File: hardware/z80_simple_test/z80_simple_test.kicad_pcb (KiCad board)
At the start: 2 copper layers, 95 x 100 mm, 50 parts, among them J1 Barrel_Jack_Switch, J2 Conn_02x15_Odd_Even, U1 Z84C000XPEG, U2 SRAM_512K8B_DIP_SOP_SOJ, U3 EEPROM_512K8B_DIP, U4 74XX138, U5 Z84C40XPEG, U6 74XX32, U7 74XX00

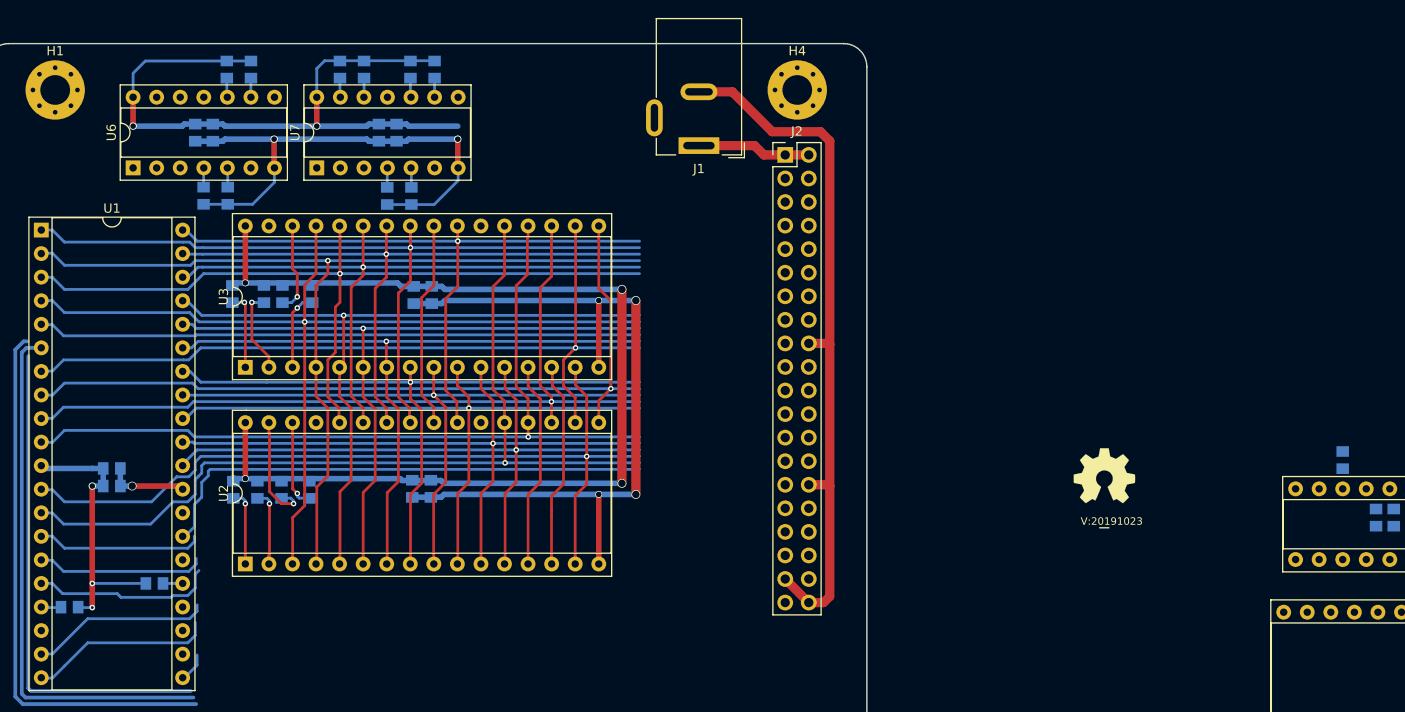
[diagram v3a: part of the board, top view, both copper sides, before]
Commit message: futher layout of the mainboard bus, replaced footprints of resistors with a bit more compact 0805/0603 universal footprint
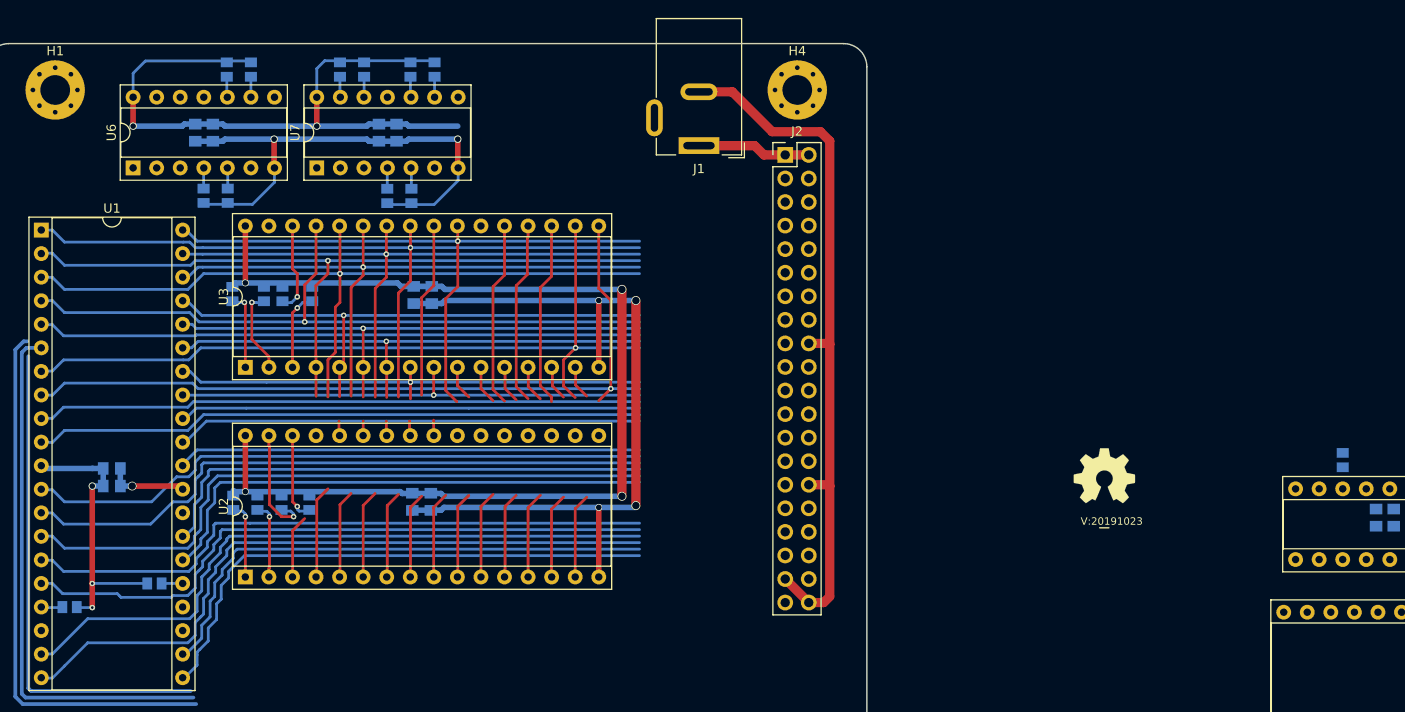
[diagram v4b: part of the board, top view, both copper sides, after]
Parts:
- R1, R10, R11, R12, R13, R14, R15, R16, R17, R18, R19, R2, R20, R21, R3, R4, R5, R6, R7, R8, R9: footprint SquantorRcl:C_0805+0603 -> SquantorRcl:R_0805+0603
- moved C3 1.40 mm to (148.5, 99.4)
- moved C4 1.40 mm to (150.5, 99.4)
- moved R4 1.40 mm to (131.8, 99.5)
- moved R5 1.40 mm to (129.2, 99.5)
- moved R6 1.40 mm to (137.4, 99.5)
- moved R7 1.40 mm to (134.4, 99.5)
- moved U2 1.40 mm to (130.5, 107.5)
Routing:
- net /!WR: track 1.18 -> 58.5 mm
- net /!RD: track 3.52 -> 58.9 mm
- net /!RESET: track 0.30 -> 55.4 mm
- net /!IORQ: track 19.9 -> 74.0 mm
- net /!MREQ: track 19.4 -> 72.5 mm
- net /!INT: track 19.7 -> 70.1 mm
- net /D0: track 40.2 -> 84.3 mm
- net /D1: track 40.4 -> 81.4 mm
- net /A14: track 103.0 -> 83.2 mm
- net /A3: track 71.6 -> 61.6 mm
- net /A4: track 72.2 -> 62.6 mm
- net /A5: track 74.6 -> 65.0 mm
- net /A7: track 77.9 -> 68.4 mm
- net /A6: track 76.0 -> 66.4 mm
- net /D2: track 89.8 -> 80.3 mm, vias 1 -> 0
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
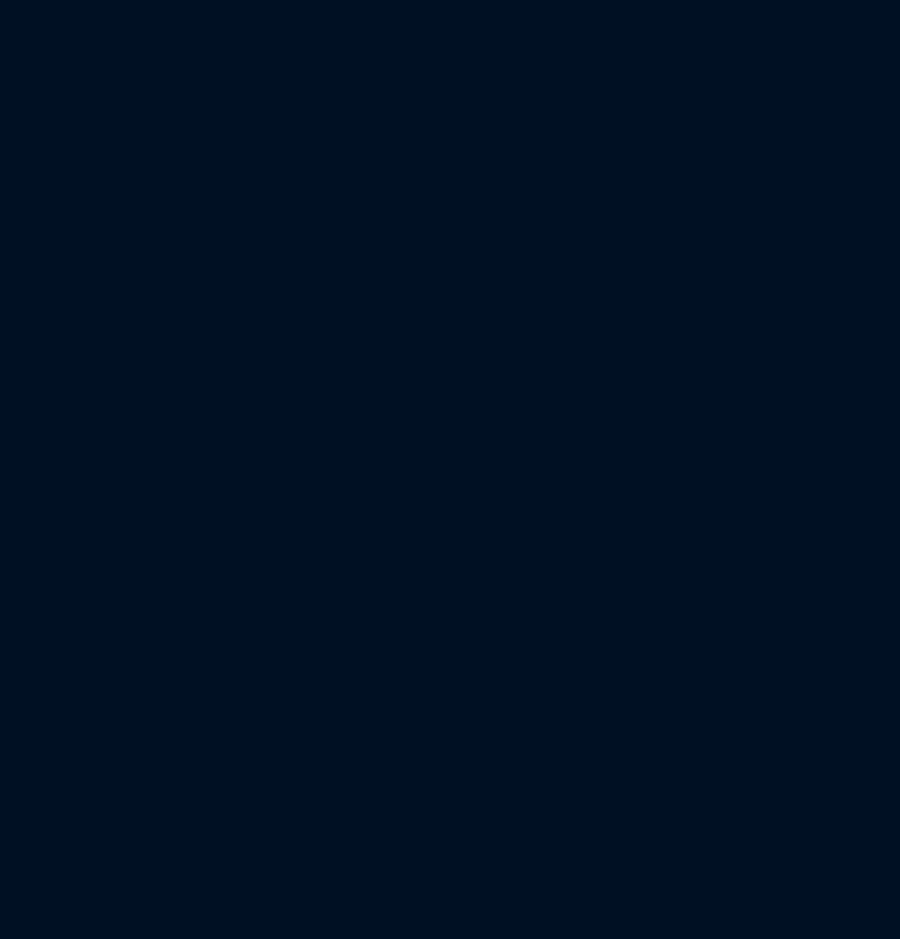
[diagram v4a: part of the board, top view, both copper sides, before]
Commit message: added power switch, need to rethink layout (again)
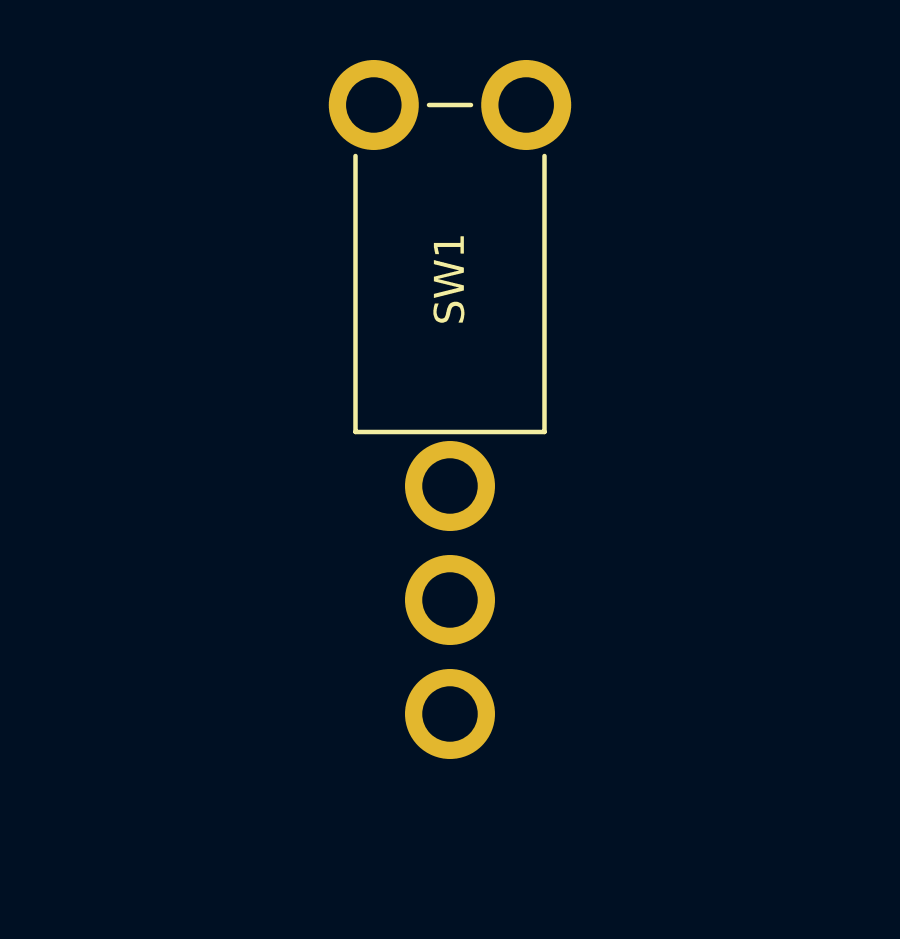
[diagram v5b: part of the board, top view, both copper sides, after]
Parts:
- added SW1: SW_Push_SPDT, SquantorSwitches:MS_500AVT, F.Cu at (227.2, 61.4)
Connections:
- J1 pad 1: /VDD -> Net-(J1-Pad1)
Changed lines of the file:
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@@
     (tracks 646)
     (zones 0)
-    (modules 50)
-    (nets 62)
+    (modules 51)
+    (nets 63)
   )
   (page A4)
@@
   (net 60 "Net-(R21-Pad2)")
   (net 61 /!RAM_CE)
+  (net 62 "Net-(J1-Pad1)")
   (net_class Default "This is the default net class."
     (clearance 0.2)
@@
     (add_net /D7)
     (add_net /SEL_SIO)
+    (add_net "Net-(J1-Pad1)")
     (add_net "Net-(J1-Pad3)")
     (add_net "Net-(R1-Pad2)")
@@
     (add_net "Net-(R20-Pad2)")
     (add_net "Net-(R21-Pad2)")
+    (add_net "Net-(SW1-Pad3)")
     (add_net "Net-(U1-Pad23)")
     (add_net "Net-(U1-Pad28)")
@@
     (add_net /VSS)
   )
+  (module SquantorSwitches:MS_500AVT (layer F.Cu)
+    (at 227.2 61.4 270)
+    (fp_text reference SW1 (at -6.9 0 90) (layer F.SilkS)
+      (effects (font (size 1 1) (thickness 0.15)))
+    )
+    (fp_text value SW_Push_SPDT (at 0 -0.5 90) (layer F.Fab)
+      (effects (font (size 1 1) (thickness 0.15)))
+    )
+    (fp_line (start -11 -3.15) (end -1.8 -3.15) (layer F.SilkS) (width 0.15))
+    (fp_line (start -12.7 0.7) (end -12.7 -0.7) (layer F.SilkS) (width 0.15))
+    (fp_line (start -1.8 3.15) (end -11 3.15) (layer F.SilkS) (width 0.15))
+    (fp_line (start -1.8 -3.15) (end -1.8 3.15) (layer F.SilkS) (width 0.15))
+    (fp_arc (start -30.8 0) (end -30.8 -1.5) (angle -180) (layer Dwgs.User) (width 0.1))
+    (fp_line (start -20.6 1) (end -30.8 1.5) (layer Dwgs.User) (width 0.1))
+    (fp_line (start -30.8 -1.5) (end -20.6 -1) (layer Dwgs.User) (width 0.1))
+    (fp_line (start -20.6 3) (end -12.7 3) (layer Dwgs.User) (width 0.1))
+    (fp_line (start -20.6 -3) (end -12.7 -3) (layer Dwgs.User) (width 0.1))
+    (fp_line (start -20.6 -3) (end -20.6 3) (layer Dwgs.User) (width 0.1))
+    (fp_line (start 8.2 0.5) (end -1.8 0.5) (layer Dwgs.User) (width 0.1))
+    (fp_line (start 8.2 -0.5) (end -1.8 -0.5) (layer Dwgs.User) (width 0.1))
+    (fp_line (start 8.2 -0.5) (end 8.2 0.5) (layer Dwgs.User) (width 0.1))
+    (fp_line (start -1.8 -3.15) (end -1.8 3.15) (layer Dwgs.User) (width 0.1))
+    (fp_line (start -12.7 3.15) (end -1.8 3.15) (layer Dwgs.User) (width 0.1))
+    (fp_line (start -12.7 -3.15) (end -1.8 -3.15) (layer Dwgs.User) (width 0.1))
+    (fp_line (start -12.7 3.15) (end -12.7 -3.15) (layer Dwgs.User) (width 0.1))
+    (pad S thru_hole circle (at -12.7 -2.54 270) (size 3 3) (drill 1.85) (layers *.Cu *.Mask))
+    (pad S thru_hole circle (at -12.7 2.54 270) (size 3 3) (drill 1.85) (layers *.Cu *.Mask))
+    (pad 3 thru_hole circle (at 7.6 0 270) (size 3 3) (drill 1.85) (layers *.Cu *.Mask))
+    (pad 2 thru_hole circle (at 3.8 0 270) (size 3 3) (drill 1.85) (layers *.Cu *.Mask)
+      (net 62 "Net-(J1-Pad1)"))
+    (pad 1 thru_hole circle (at 0 0 270) (size 3 3) (drill 1.85) (layers *.Cu *.Mask)
+      (net 2 /VDD))
+  )
   (module SquantorRcl:R_0805+0603 (layer B.Cu)
     (at 150.9 52.8 270)
@@
     (fp_line (start 5 14.1) (end 5 5.5) (layer F.CrtYd) (width 0.05))
     (pad 1 thru_hole rect (at 0 0 180) (size 4.4 1.8) (drill oval 3.4 0.8) (layers *.Cu *.Mask)
-      (net 2 /VDD))
+      (net 62 "Net-(J1-Pad1)"))
     (pad 2 thru_hole oval (at 0 5.8 180) (size 4 1.8) (drill oval 3 0.8) (layers *.Cu *.Mask)
       (net 1 /VSS))

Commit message: further routing
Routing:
- net /!MREQ: track 72.5 -> 147.5 mm, vias 0 -> 1
- net /!RD: track 58.9 -> 127.9 mm
- net /!WR: track 58.5 -> 116.2 mm
- net /!WAIT: track 0.32 -> 53.9 mm
- net /!MEM_WR: track 0.00 -> 42.7 mm
- net /!MEM_RD: track 20.5 -> 60.6 mm
- net /!RAM_CE: track 0.00 -> 39.6 mm
- net /A15: track 65.1 -> 99.1 mm, vias 0 -> 2
- net /A14: track 83.2 -> 105.2 mm, vias 1 -> 2
- net /A3: track 61.6 -> 73.0 mm
- net /A4: track 62.6 -> 73.6 mm
- net /A5: track 65.0 -> 76.0 mm
- net /A7: track 68.4 -> 79.3 mm
- net /A6: track 66.4 -> 77.4 mm
- net /D2: track 80.3 -> 91.2 mm, vias 0 -> 1
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
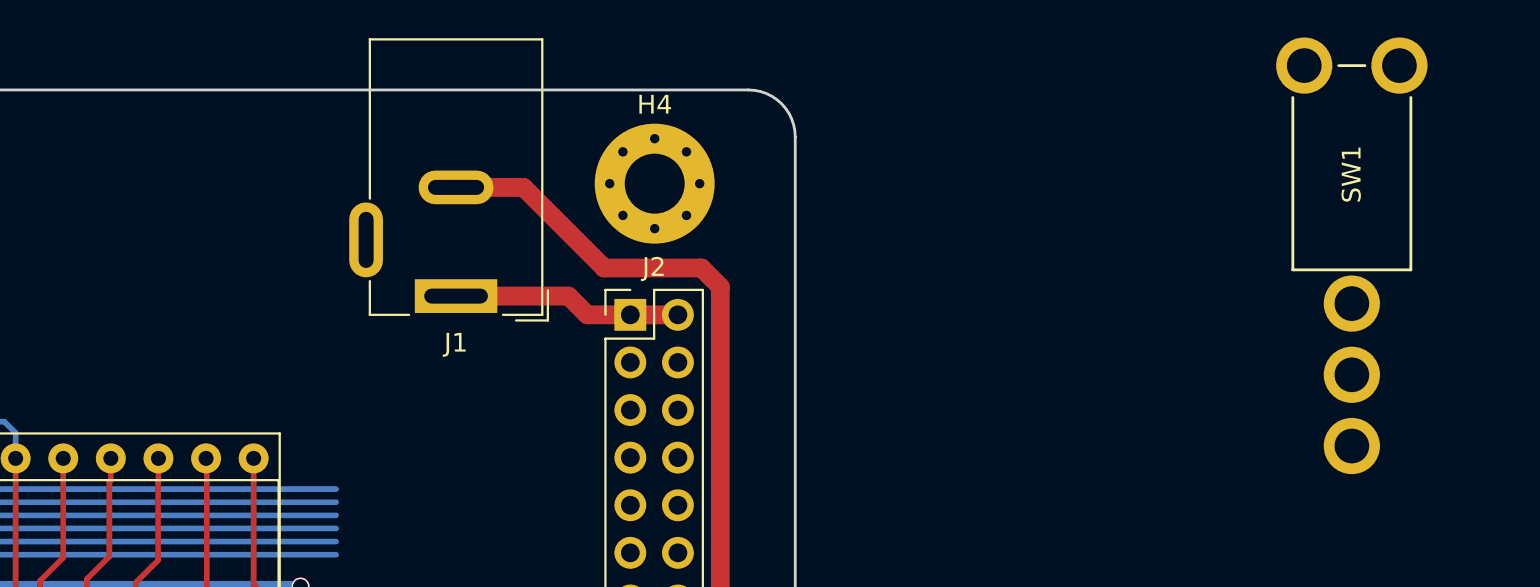
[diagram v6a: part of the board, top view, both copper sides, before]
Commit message: added capacitor and removed power switch, it is just a test
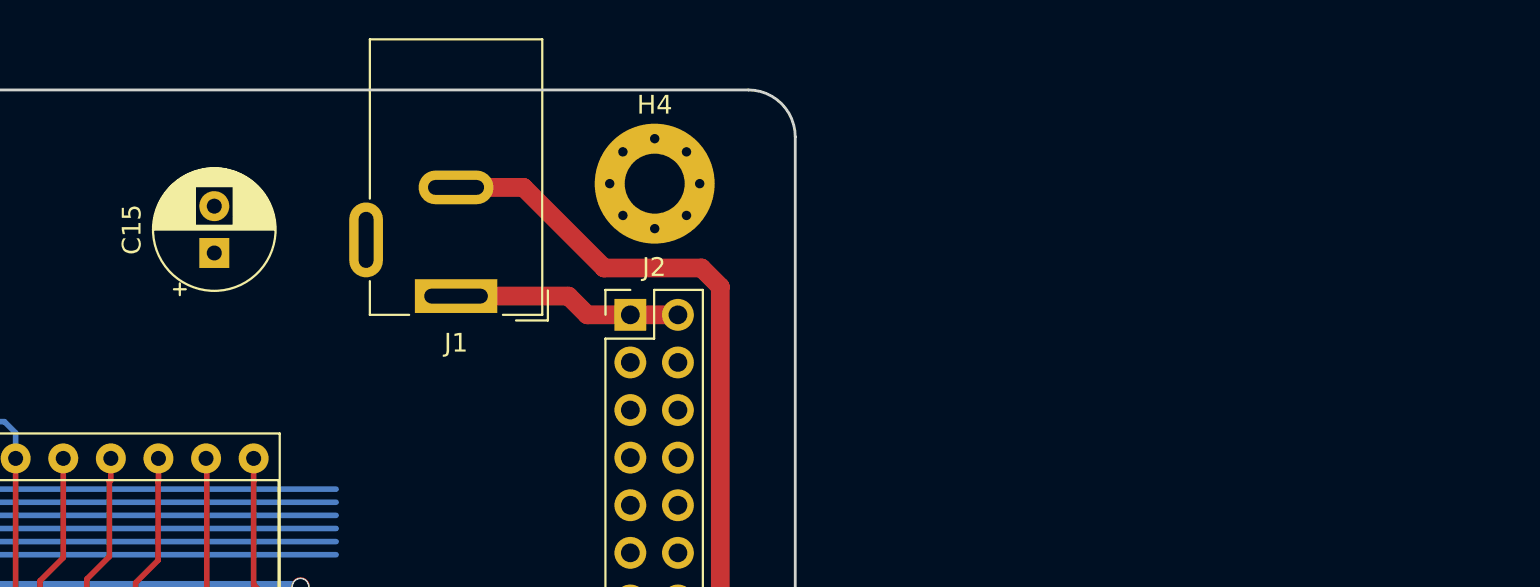
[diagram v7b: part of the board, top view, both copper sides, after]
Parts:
- removed SW1: SW_Push_SPDT, SquantorSwitches:MS_500AVT
- added C15: CP, Capacitor_THT:CP_Radial_D6.3mm_P2.50mm, F.Cu at (166.5, 58.7)
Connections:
- J1 pad 1: Net-(J1-Pad1) -> /VDD
